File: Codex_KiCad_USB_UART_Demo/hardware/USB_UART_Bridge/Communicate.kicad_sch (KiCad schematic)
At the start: 15 parts, among them U1 CH343G, U3 ISO7721D

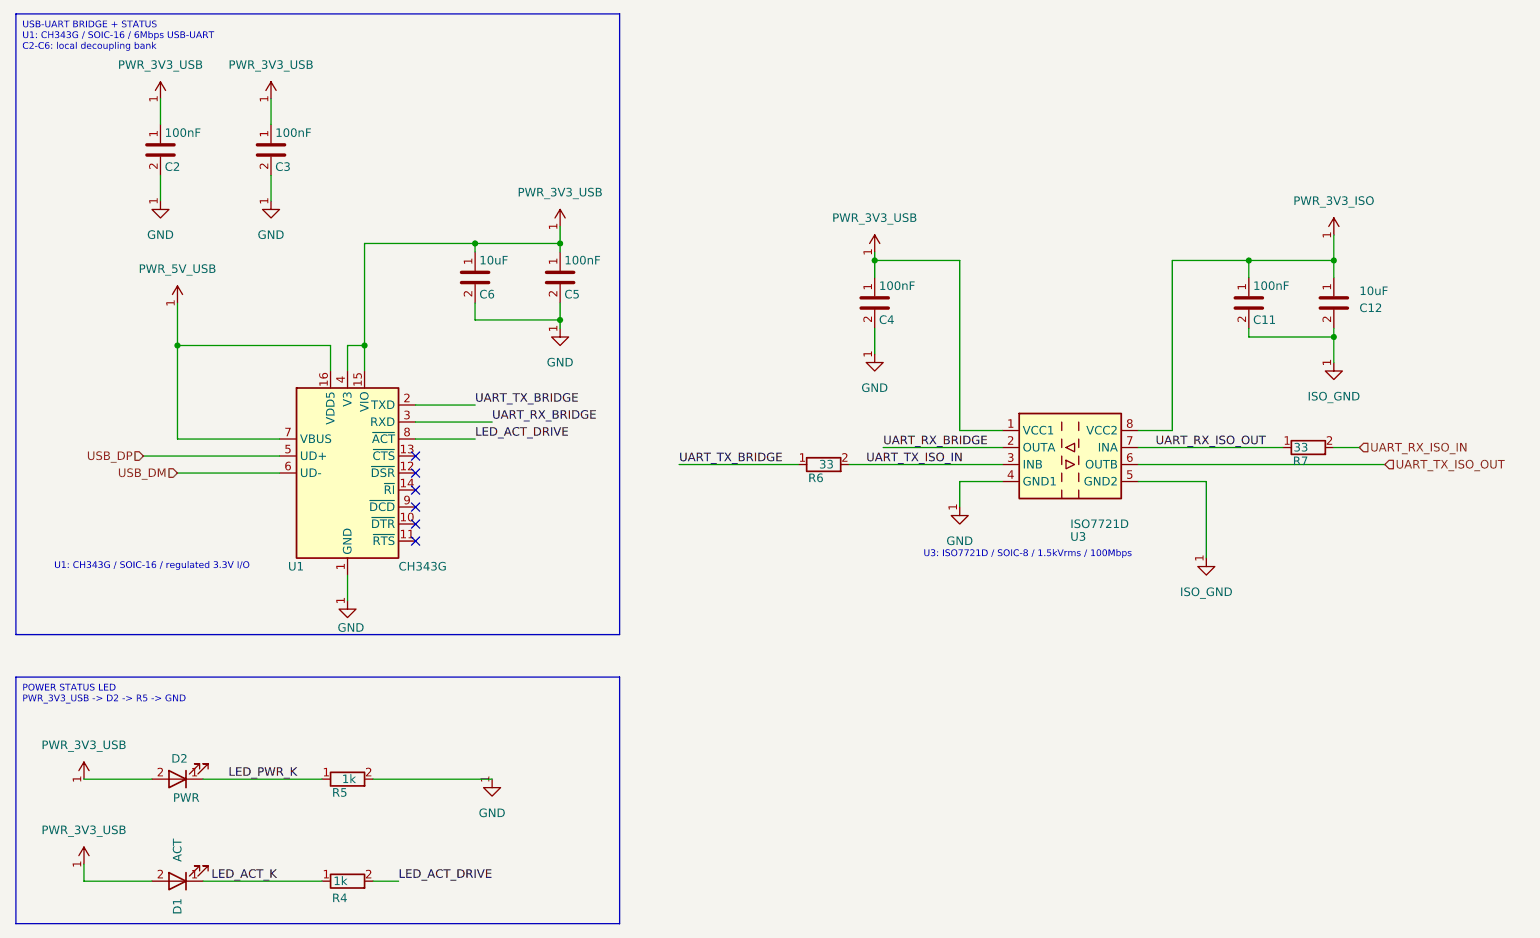
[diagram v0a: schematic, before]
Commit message: feat: complete USB UART PCB layout and routing
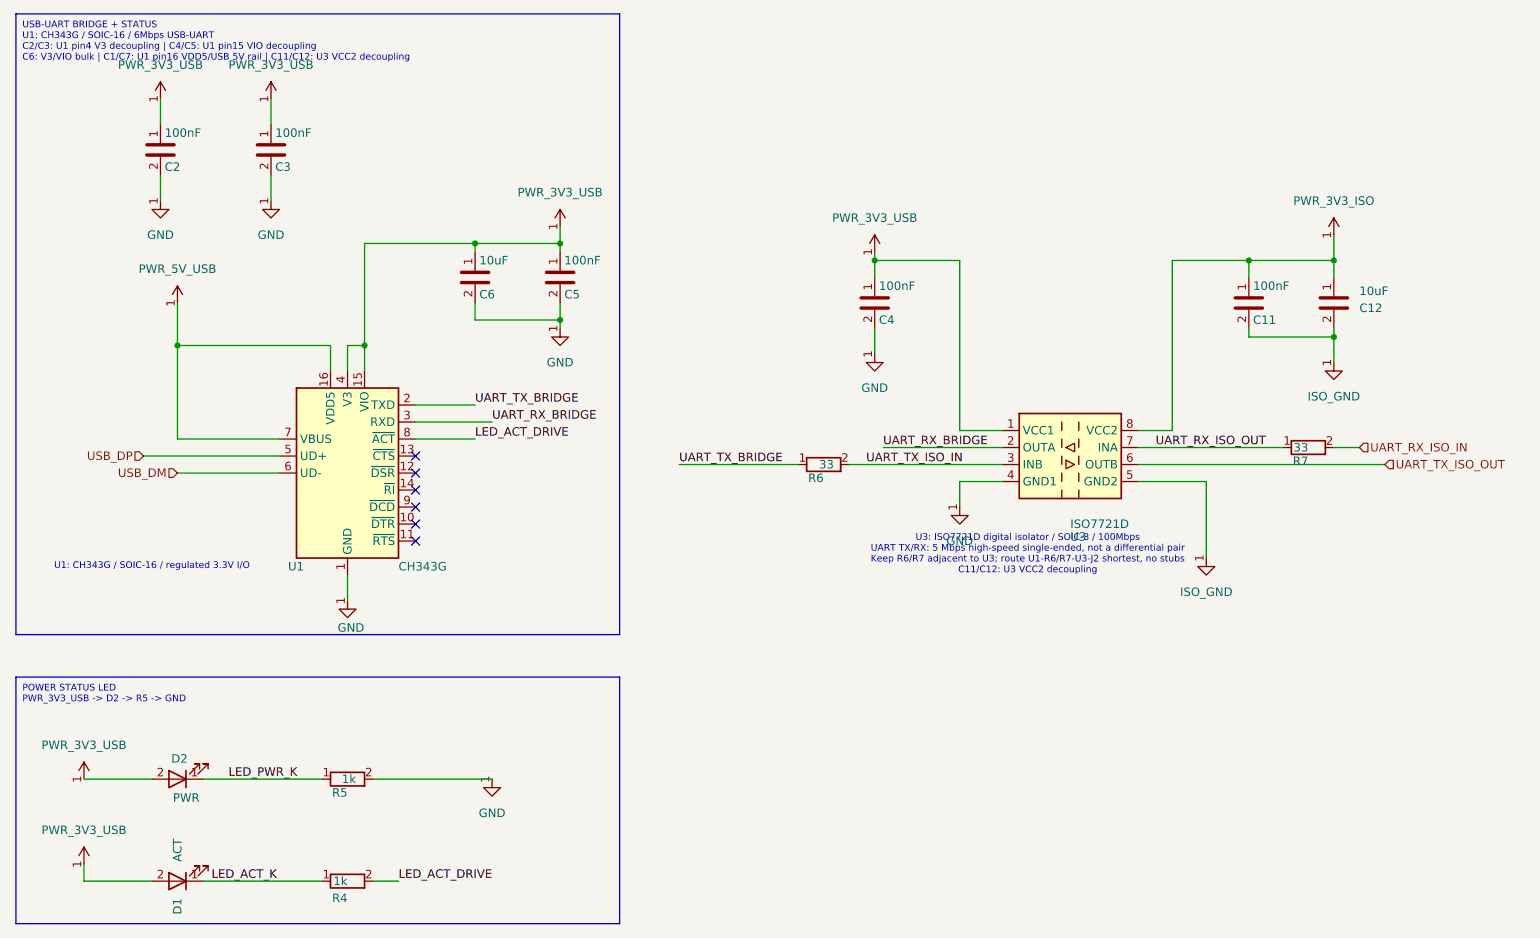
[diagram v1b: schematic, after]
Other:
- note added: "U3: ISO7721D digital isolator / SOIC-8 / 100Mbps UART TX/RX: 5 Mbps high-speed single-ended, not a differential pair Keep R6/R7 adjacent to U3; route U1-R6/R7-U3-J2 shortest, no stubs C11/C12: U3 VCC2 decoupling"
- note removed: "U3: ISO7721D / SOIC-8 / 1.5kVrms / 100Mbps"
